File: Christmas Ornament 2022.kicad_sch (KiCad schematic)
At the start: 52 parts, among them J1 USB_B_Micro, SW1 SW_Push, SW2 SW_Push, U1 AMS1117-3.3, U2 RP2040, U3 MCP9700T-ETT, U4 TPS61040DBV

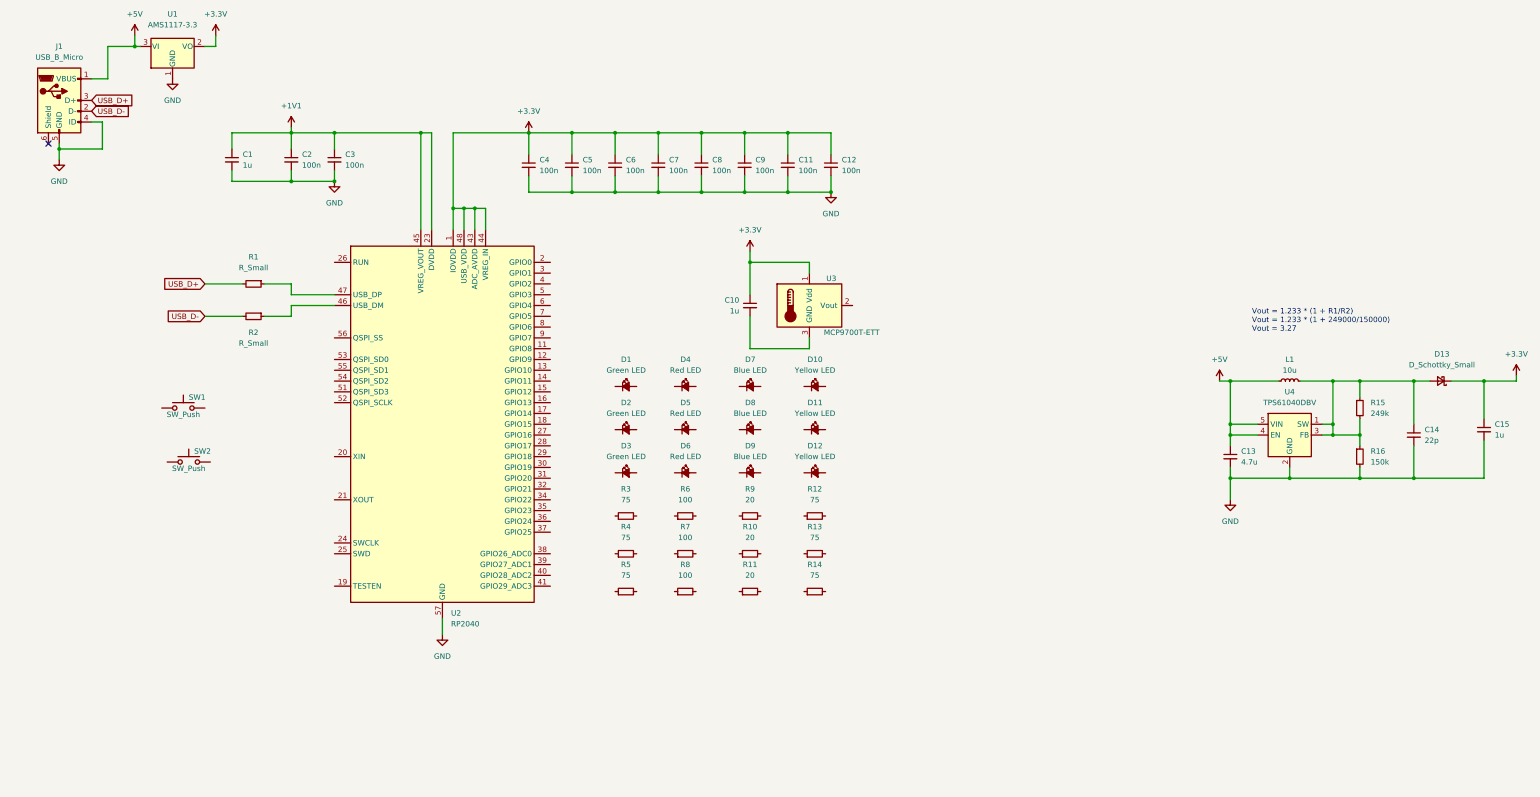
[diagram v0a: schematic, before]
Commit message: Added flash and connected IO
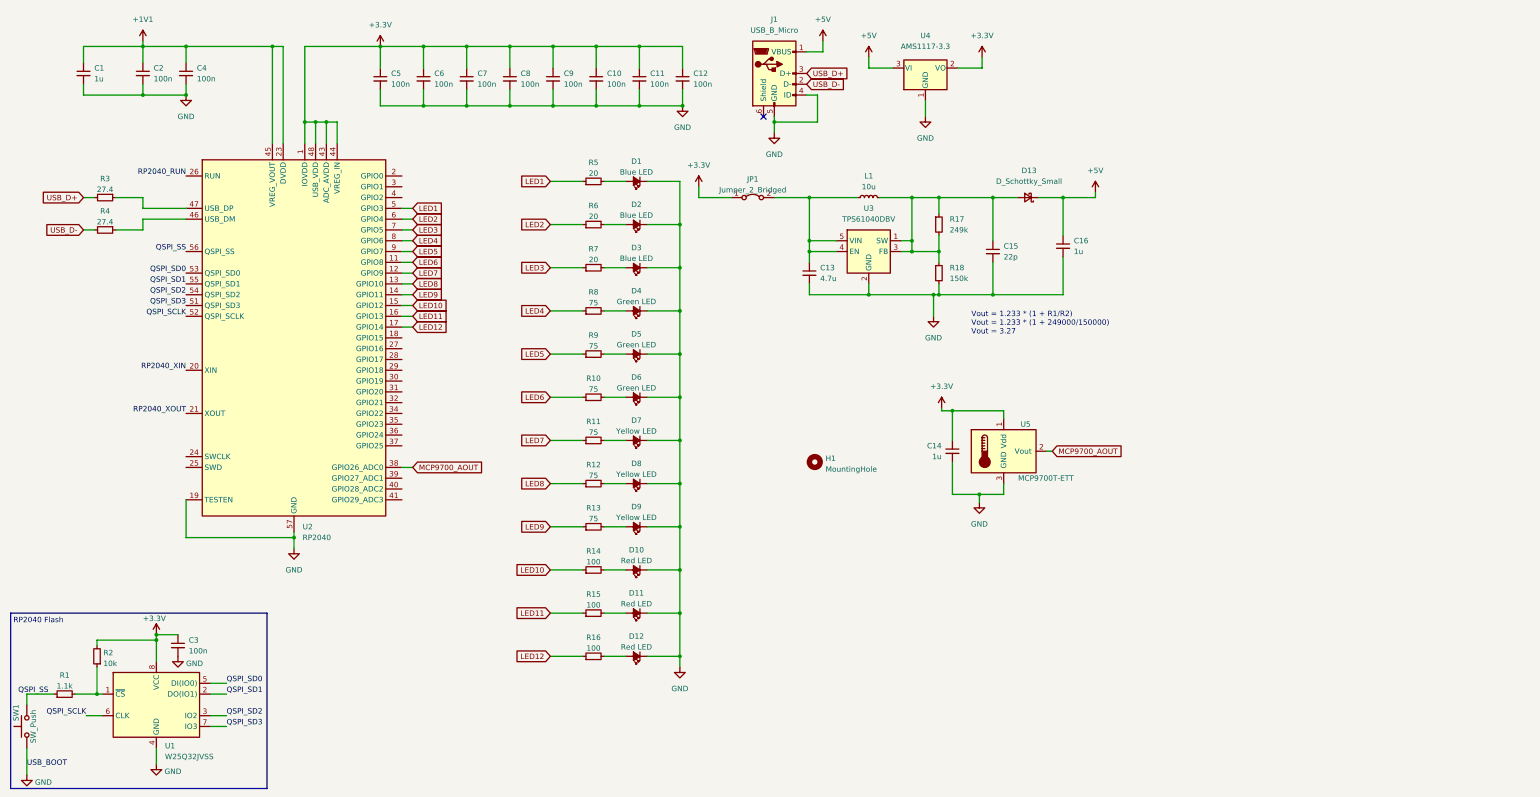
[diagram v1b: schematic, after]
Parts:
- removed SW2: SW_Push, Ornament Footprints:TS-1187A-B-A-B, symbol Switch:SW_Push
- added C3: 100n, Capacitor_SMD:C_0805_2012Metric, symbol Device:C_Small
- added H1: MountingHole, MountingHole:MountingHole_3.2mm_M3, symbol Mechanical:MountingHole
- added JP1: Jumper_2_Bridged, Jumper:SolderJumper-2_P1.3mm_Bridged_Pad1.0x1.5mm, symbol Jumper:Jumper_2_Bridged
- added R1: 1.1k, Resistor_SMD:R_0603_1608Metric, symbol Device:R_Small
- added R4: 27.4, Resistor_SMD:R_0402_1005Metric, symbol Device:R_Small
- added U1: W25Q32JVSS, Package_SO:SOIC-8_5.23x5.23mm_P1.27mm, symbol Memory_Flash:W25Q32JVSS
- J1: footprint (none) -> Connector_USB:USB_Micro-B_Amphenol_10118194_Horizontal; Part Number (none) -> C132563; Vendor (none) -> JLCPCB
- R2: value R_Small -> 10k; footprint (none) -> Resistor_SMD:R_0603_1608Metric; Part Number (none) -> C25804; Vendor (none) -> JLCPCB
- R3: renamed from R1; value R_Small -> 27.4; footprint (none) -> Resistor_SMD:R_0402_1005Metric; Part Number (none) -> C172043; Vendor (none) -> JLCPCB
- renumbered C9 to C10, C10 to C14, C14 to C15, C15 to C16, C3 to C4, C4 to C5, C5 to C6, C6 to C7, C7 to C8, C8 to C9, D7 to D1, D4 to D10, D5 to D11, D6 to D12, D8 to D2, D9 to D3, D1 to D4, D2 to D5, D3 to D6, D10 to D7, D11 to D8, D12 to D9, R5 to R10, R12 to R11, R13 to R12, R14 to R13, R6 to R14, R7 to R15, R8 to R16, R15 to R17, R16 to R18, R9 to R5, R10 to R6, R11 to R7, R3 to R8, R4 to R9, U4 to U3, U1 to U4, U3 to U5
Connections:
- net +3.3V: now also R2.2, C3.1, JP1.1 (A), U1.8 (VCC); no longer C16.1, D13.1 (K)
- net +5V: now also C16.1, D13.1 (K); no longer C13.1, L1.1, U3.4 (EN), U3.5 (VIN)
- net GND: now also C14.2, D1.1 (K), D10.1 (K), D11.1 (K), D12.1 (K), D2.1 (K), D3.1 (K), D4.1 (K), D5.1 (K), D6.1 (K), D7.1 (K), D8.1 (K), D9.1 (K), SW1.1, U2.19 (TESTEN), U5.3 (GND), C3.2, U1.4 (GND)
- net USB_D-: now also R4.2; no longer R2.2
- net LED1: now reaches R5.1
- net LED1: now also U2.5 (GPIO3)
- net at R5.2: now also D1.2 (A)
- net LED9: now reaches R13.1
- net LED9: now also U2.14 (GPIO11)
- net at R13.2: now also D9.2 (A)
- net QSPI_SS: now reaches SW1.2
- net QSPI_SS: now also U2.56 (QSPI_SS), R1.1
- net LED5: now reaches R9.1
- net LED5: now also U2.9 (GPIO7)
- net at R9.2: now also D5.2 (A)
- net at D8.2 (A): now also R12.2
- net MCP9700_AOUT: now reaches U5.2 (Vout)
- net MCP9700_AOUT: now also U2.38 (GPIO26_ADC0)
- net at D3.2 (A): now also R7.2
- net at D12.2 (A): now also R16.2
- net LED4: now reaches R8.1
- net LED4: now also U2.8 (GPIO6)
- net at R8.2: now also D4.2 (A)
- net at D11.2 (A): now also R15.2
- net LED3: now reaches R7.1
- net LED3: now also U2.7 (GPIO5)
- net LED12: now reaches R16.1
- net LED12: now also U2.17 (GPIO14)
- net LED6: now reaches R10.1
- net LED6: now also U2.11 (GPIO8)
- net at R10.2: now also D6.2 (A)
- net LED7: now reaches U2.12 (GPIO9)
- net LED7: now also R11.1
- net LED8: now reaches U2.13 (GPIO10)
- net LED8: now also R12.1
- net LED10: now reaches U2.15 (GPIO12)
- net LED10: now also R14.1
- net LED11: now reaches U2.16 (GPIO13)
- net LED11: now also R15.1
- net RP2040_XIN: now reaches U2.20 (XIN)
- net RP2040_XOUT: now reaches U2.21 (XOUT)
- net RP2040_RUN: now reaches U2.26 (RUN)
- net at R2.1: now also R1.2, U1.1 (~{CS}); no longer U2.46 (USB_DM)
- net QSPI_SD3: now reaches U2.51 (QSPI_SD3)
- net QSPI_SD3: now also U1.7 (IO3)
- net QSPI_SCLK: now reaches U2.52 (QSPI_SCLK)
- net QSPI_SCLK: now also U1.6 (CLK)
- net QSPI_SD0: now reaches U2.53 (QSPI_SD0)
- net QSPI_SD0: now also U1.5 (DI(IO0))
- net QSPI_SD2: now reaches U2.54 (QSPI_SD2)
- net QSPI_SD2: now also U1.3 (IO2)
- net QSPI_SD1: now reaches U2.55 (QSPI_SD1)
- net QSPI_SD1: now also U1.2 (DO(IO1))
- net LED2: now reaches U2.6 (GPIO4)
- net LED2: now also R6.1
- net at D2.2 (A): now also R6.2
- net at R14.2: now also D10.2 (A)
- net at D7.2 (A): now also R11.2
- new net: C13.1, JP1.2 (B), L1.1, U3.4 (EN), U3.5 (VIN)
- new net: R4.1, U2.46 (USB_DM)
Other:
- note added: "RP2040 Flash"
- company: (none) -> github.com/jacobantoun
- title: (none) -> Christmas Ornament 2022
- moved on the sheet: C1, C10, C11, C12, C13, C14, C15, C16, C2, C4, C5, C6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

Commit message: Finished layout
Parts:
- added C17, C18: 30p, Capacitor_SMD:C_0402_1005Metric, symbol Device:C_Small
- added D14: Green PWR LED, LED_SMD:LED_0603_1608Metric, symbol Device:LED_Small_Filled
- added J2, J4: Conn_01x03, Connector_PinHeader_1.00mm:PinHeader_1x03_P1.00mm_Vertical, symbol Connector_Generic:Conn_01x03
- added J3: Battery Input, Connector_PinHeader_2.54mm:PinHeader_1x02_P2.54mm_Vertical, symbol Connector_Generic:Conn_01x02
- added R19: 180, Resistor_SMD:R_0603_1608Metric, symbol Device:R_Small
- added R20: 1.1k, Resistor_SMD:R_0603_1608Metric, symbol Device:R_Small
- added Y1: 12MHz, Crystal:Crystal_SMD_3225-4Pin_3.2x2.5mm, symbol Device:Crystal_Small
- C10, C11, C12, C2, C3, C4, C5, C6, C7, C8, C9: footprint Capacitor_SMD:C_0805_2012Metric -> Capacitor_SMD:C_0402_1005Metric; Part Number C49678 -> C60474
- JP1: now left out of the parts list
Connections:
- net +3.3V: no longer JP1.1 (A)
- net +5V: now also C15.1, R17.1, R19.2
- net GND: now also C17.1, C18.1, D14.1 (K), J2.3 (Pin_3), J3.2 (Pin_2), J4.3 (Pin_3); no longer C15.2
- net LED1: now also U2.17 (GPIO14); no longer U2.5 (GPIO3)
- net LED10: now also U2.35 (GPIO23); no longer U2.15 (GPIO12)
- net LED11: now also U2.36 (GPIO24); no longer U2.16 (GPIO13)
- net LED12: now also U2.37 (GPIO25); no longer U2.17 (GPIO14)
- net LED2: now also U2.18 (GPIO15); no longer U2.6 (GPIO4)
- net LED3: now also U2.27 (GPIO16); no longer U2.7 (GPIO5)
- net LED4: now also U2.28 (GPIO17); no longer U2.8 (GPIO6)
- net LED5: now also U2.29 (GPIO18); no longer U2.9 (GPIO7)
- net LED6: now also U2.30 (GPIO19); no longer U2.11 (GPIO8)
- net LED7: now also U2.31 (GPIO20); no longer U2.12 (GPIO9)
- net LED8: now also U2.32 (GPIO21); no longer U2.13 (GPIO10)
- net LED9: now also U2.34 (GPIO22); no longer U2.14 (GPIO11)
- net RP2040_XIN: now also C17.2, Y1.2
- net RP2040_XOUT: now also R20.2
- net UART0_TX: now reaches U2.2 (GPIO0)
- net UART0_TX: now also J2.1 (Pin_1)
- net DBG_SWCLK: now reaches U2.24 (SWCLK)
- net DBG_SWCLK: now also J4.1 (Pin_1)
- net DBG_SWD: now reaches U2.25 (SWD)
- net DBG_SWD: now also J4.2 (Pin_2)
- net UART0_RX: now reaches U2.3 (GPIO1)
- net UART0_RX: now also J2.2 (Pin_2)
- new net: C18.2, R20.1, Y1.1
- new net: C15.2, R17.2, R18.1, U3.3 (FB)
- new net: D14.2 (A), R19.1
- new net: D13.2 (A), L1.2, U3.1 (SW)
- new net +BATT: J3.1 (Pin_1), JP1.1 (A)
- no-connect marks 1 -> 16
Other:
- moved on the sheet: C1, C10, C11, C12, C13, C14, C15, C16, C2, C4, C5, C6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
